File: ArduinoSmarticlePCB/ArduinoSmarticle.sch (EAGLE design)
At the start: 22 parts, among them U1 LSM6DS3DOT_INDICATION

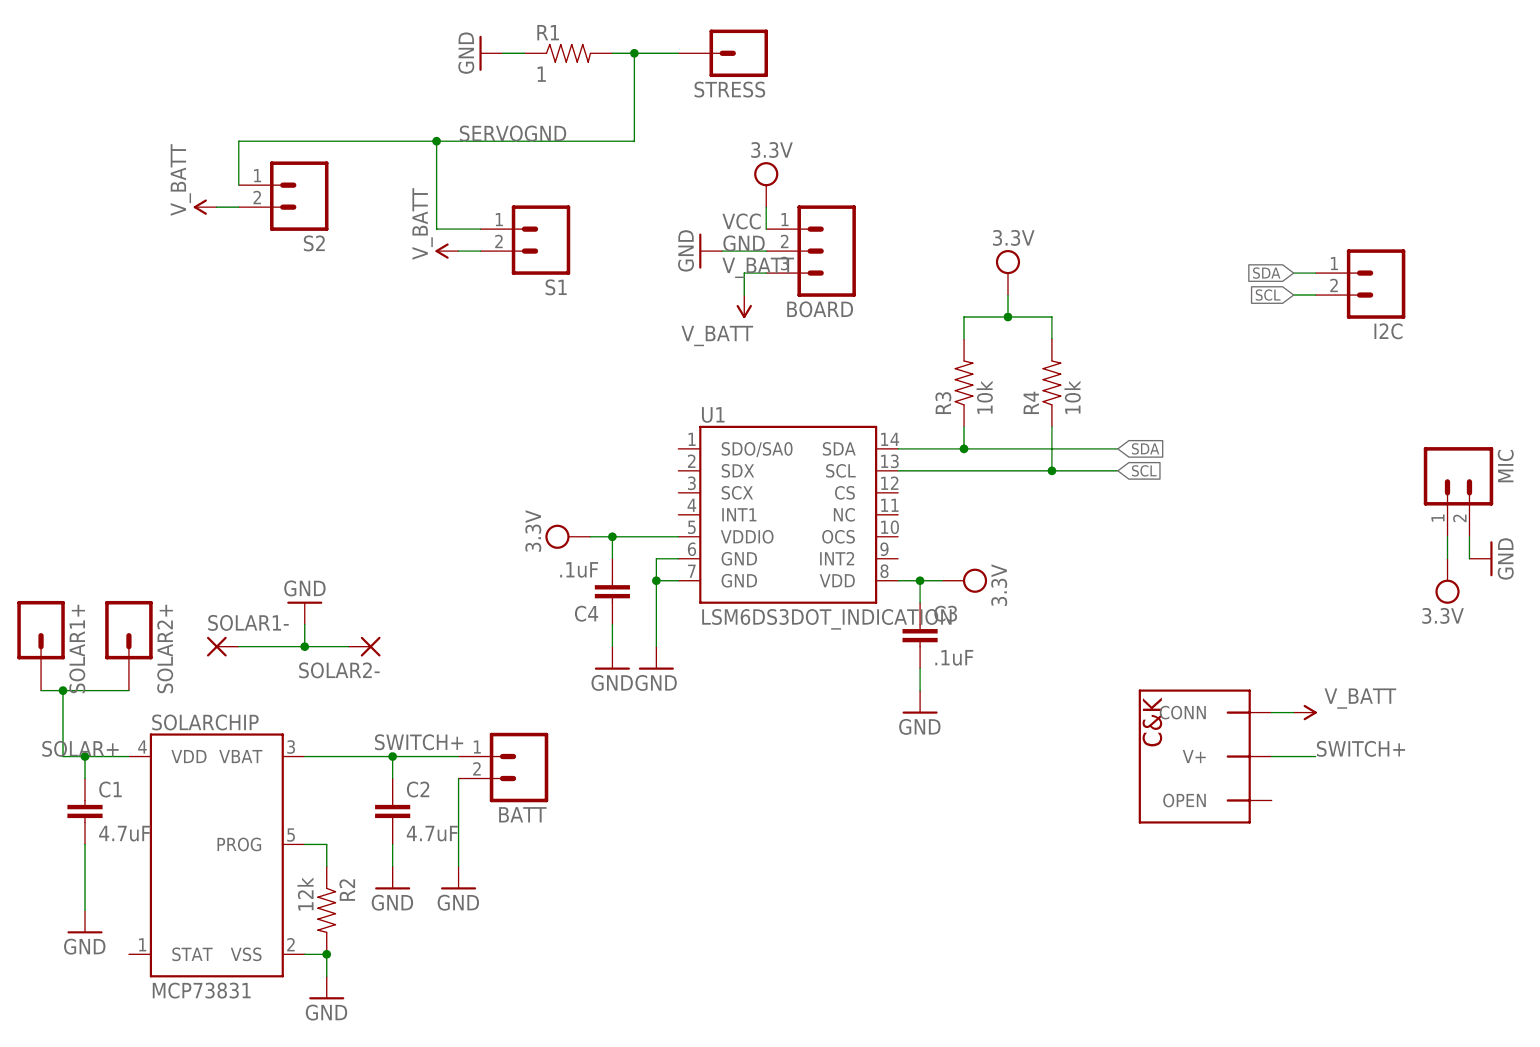
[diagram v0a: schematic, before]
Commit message: improved size of board and isolation size, added mathematica notebook describing solar panels
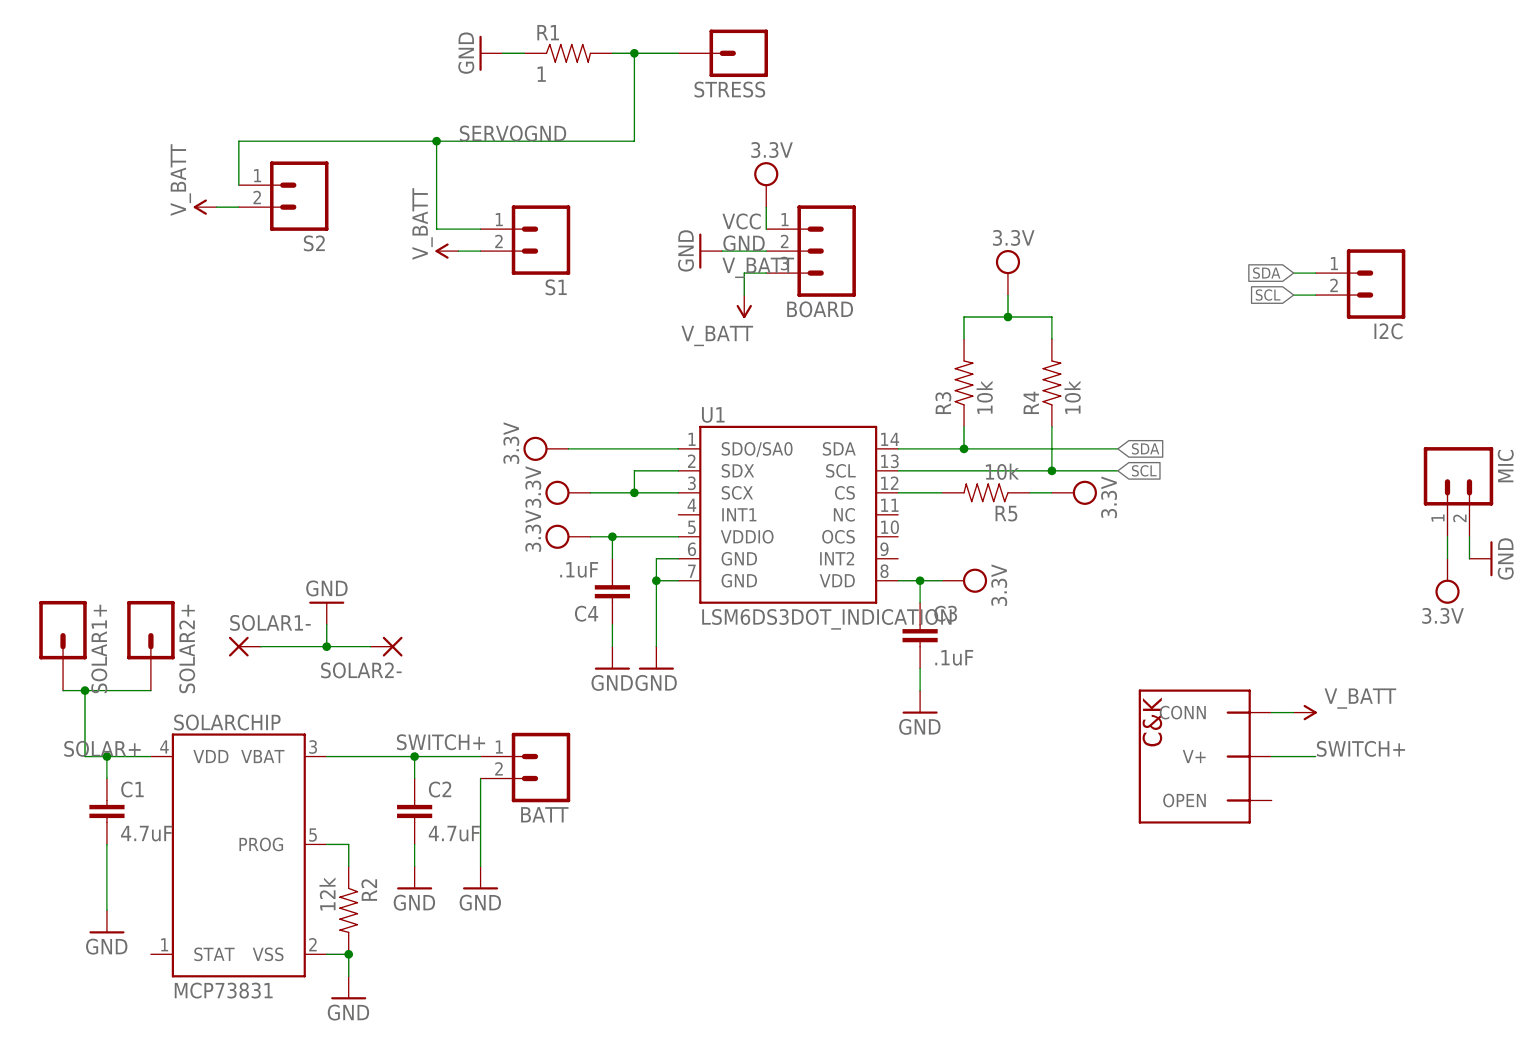
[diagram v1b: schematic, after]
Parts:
- added R5: 10k, SparkFun-Resistors:4.7KOHM-1/10W-1%(0603)
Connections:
- new net N$2: R5.2, U1.CS
- net VCC: now also R5.1, U1.SCX, U1.SDO/SA0, U1.SDX
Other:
- moved on the sheet: BATT, C1, C2, R2, SOLAR1+, SOLAR1-, SOLAR2+, SOLAR2-, SOLARCHIP
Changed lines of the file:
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@@
 <part name="GND11" library="SparkFun-Aesthetics" deviceset="GND" device=""/>
 <part name="I2C" library="SparkFun-Connectors" deviceset="M02" device="PTH"/>
+<part name="R5" library="SparkFun-Resistors" deviceset="4.7KOHM-1/10W-1%(0603)" device="" value="10k"/>
+<part name="3.3V5" library="supply2" deviceset="VCC" device="" value="3.3V"/>
+<part name="3.3V6" library="supply2" deviceset="VCC" device="" value="3.3V"/>
+<part name="3.3V7" library="supply2" deviceset="VCC" device="" value="3.3V"/>
 </parts>
 <sheets>
@@
 <instances>
 <instance part="FRAME1" gate="G$1" x="0" y="0"/>
-<instance part="SOLARCHIP" gate="G$1" x="25.4" y="27.94"/>
-<instance part="C1" gate="G$1" x="10.16" y="30.48"/>
-<instance part="C2" gate="G$1" x="45.72" y="30.48"/>
-<instance part="GND1" gate="1" x="10.16" y="17.78"/>
-<instance part="GND2" gate="1" x="45.72" y="22.86"/>
-<instance part="GND4" gate="1" x="38.1" y="10.16"/>
-<instance part="R2" gate="G$1" x="38.1" y="20.32" rot="R270"/>
+<instance part="SOLARCHIP" gate="G$1" x="27.94" y="27.94"/>
+<instance part="C1" gate="G$1" x="12.7" y="30.48"/>
+<instance part="C2" gate="G$1" x="48.26" y="30.48"/>
+<instance part="GND1" gate="1" x="12.7" y="17.78"/>
+<instance part="GND2" gate="1" x="48.26" y="22.86"/>
+<instance part="GND4" gate="1" x="40.64" y="10.16"/>
+<instance part="R2" gate="G$1" x="40.64" y="20.32" rot="R270"/>
 <instance part="S2" gate="G$1" x="35.56" y="104.14" smashed="yes" rot="R180">
 <attribute name="VALUE" x="38.1" y="111.76" size="1.778" layer="96" rot="R180"/>
@@
 <instance part="GND5" gate="1" x="81.28" y="96.52" rot="R270"/>
 <instance part="SUPPLY4" gate="G$1" x="86.36" y="91.44" rot="R180"/>
-<instance part="BATT" gate="G$1" x="60.96" y="38.1" rot="R180"/>
-<instance part="GND6" gate="1" x="53.34" y="22.86"/>
-<instance part="SOLAR1+" gate="G$1" x="5.08" y="53.34" rot="R270"/>
-<instance part="SOLAR2+" gate="G$1" x="15.24" y="53.34" rot="R270"/>
-<instance part="GND3" gate="1" x="35.56" y="55.88" rot="R180"/>
-<instance part="SOLAR1-" gate="1" x="25.4" y="50.8"/>
-<instance part="SOLAR2-" gate="1" x="43.18" y="50.8" rot="R180"/>
+<instance part="BATT" gate="G$1" x="63.5" y="38.1" rot="R180"/>
+<instance part="GND6" gate="1" x="55.88" y="22.86"/>
+<instance part="SOLAR1+" gate="G$1" x="7.62" y="53.34" rot="R270"/>
+<instance part="SOLAR2+" gate="G$1" x="17.78" y="53.34" rot="R270"/>
+<instance part="GND3" gate="1" x="38.1" y="55.88" rot="R180"/>
+<instance part="SOLAR1-" gate="1" x="27.94" y="50.8"/>
+<instance part="SOLAR2-" gate="1" x="45.72" y="50.8" rot="R180"/>
 <instance part="U$1" gate="G$1" x="132.08" y="30.48"/>
 <instance part="SUPPLY1" gate="G$1" x="149.86" y="43.18" smashed="yes" rot="R270">
@@
 <instance part="GND11" gate="1" x="106.68" y="43.18"/>
 <instance part="I2C" gate="G$1" x="160.02" y="93.98" rot="R180"/>
+<instance part="R5" gate="G$1" x="114.3" y="68.58" rot="R180"/>
+<instance part="3.3V5" gate="G$1" x="124.46" y="68.58" rot="R270"/>
+<instance part="3.3V6" gate="G$1" x="66.04" y="68.58" rot="R90"/>
+<instance part="3.3V7" gate="G$1" x="63.5" y="73.66" rot="R90"/>
 </instances>
 <busses>
@@
 <pinref part="C1" gate="G$1" pin="2"/>
 <pinref part="GND1" gate="1" pin="GND"/>
-<wire x1="10.16" y1="27.94" x2="10.16" y2="20.32" width="0.1524" layer="91"/>
+<wire x1="12.7" y1="27.94" x2="12.7" y2="20.32" width="0.1524" layer="91"/>
 </segment>
 <segment>
 <pinref part="SOLARCHIP" gate="G$1" pin="VSS"/>
 <pinref part="R2" gate="G$1" pin="2"/>
-<wire x1="35.56" y1="15.24" x2="38.1" y2="15.24" width="0.1524" layer="91"/>
+<wire x1="38.1" y1="15.24" x2="40.64" y2="15.24" width="0.1524" layer="91"/>
 <pinref part="GND4" gate="1" pin="GND"/>
-<wire x1="38.1" y1="15.24" x2="38.1" y2="12.7" width="0.1524" layer="91"/>
-<junction x="38.1" y="15.24"/>
+<wire x1="40.64" y1="15.24" x2="40.64" y2="12.7" width="0.1524" layer="91"/>
+<junction x="40.64" y="15.24"/>
 </segment>
 <segment>
 <pinref part="C2" gate="G$1" pin="2"/>
 <pinref part="GND2" gate="1" pin="GND"/>
-<wire x1="45.72" y1="25.4" x2="45.72" y2="27.94" width="0.1524" layer="91"/>
+<wire x1="48.26" y1="25.4" x2="48.26" y2="27.94" width="0.1524" layer="91"/>
 </segment>
 <segment>
@@
 <pinref part="BATT" gate="G$1" pin="2"/>
 <pinref part="GND6" gate="1" pin="GND"/>
-<wire x1="53.34" y1="25.4" x2="53.34" y2="35.56" width="0.1524" layer="91"/>
+<wire x1="55.88" y1="25.4" x2="55.88" y2="35.56" width="0.1524" layer="91"/>
 </segment>
 <segment>
@@
 <segment>
 <pinref part="SOLAR1-" gate="1" pin="P"/>
-<wire x1="35.56" y1="50.8" x2="27.94" y2="50.8" width="0.1524" layer="91"/>
-<junction x="35.56" y="50.8"/>
+<wire x1="38.1" y1="50.8" x2="30.48" y2="50.8" width="0.1524" layer="91"/>
+<junction x="38.1" y="50.8"/>
 <pinref part="SOLAR2-" gate="1" pin="P"/>
-<wire x1="40.64" y1="50.8" x2="35.56" y2="50.8" width="0.1524" layer="91"/>
+<wire x1="43.18" y1="50.8" x2="38.1" y2="50.8" width="0.1524" layer="91"/>
 <pinref part="GND3" gate="1" pin="GND"/>
-<wire x1="35.56" y1="50.8" x2="35.56" y2="53.34" width="0.1524" layer="91"/>
+<wire x1="38.1" y1="50.8" x2="38.1" y2="53.34" width="0.1524" layer="91"/>
 </segment>
 </net>
@@
 <segment>
 <pinref part="SOLARCHIP" gate="G$1" pin="PROG"/>
-<wire x1="35.56" y1="27.94" x2="38.1" y2="27.94" width="0.1524" layer="91"/>
+<wire x1="38.1" y1="27.94" x2="40.64" y2="27.94" width="0.1524" layer="91"/>
 <pinref part="R2" gate="G$1" pin="1"/>
-<wire x1="38.1" y1="27.94" x2="38.1" y2="25.4" width="0.1524" layer="91"/>
+<wire x1="40.64" y1="27.94" x2="40.64" y2="25.4" width="0.1524" layer="91"/>
 </segment>
 </net>
@@
 <junction x="106.68" y="58.42"/>
 <wire x1="106.68" y1="58.42" x2="109.22" y2="58.42" width="0.1524" layer="91"/>
+</segment>
+<segment>
+<pinref part="R5" gate="G$1" pin="1"/>
+<pinref part="3.3V5" gate="G$1" pin="VCC"/>
+<wire x1="121.92" y1="68.58" x2="119.38" y2="68.58" width="0.1524" layer="91"/>
+</segment>
+<segment>
+<pinref part="U1" gate="G$1" pin="SCX"/>
+<wire x1="78.74" y1="68.58" x2="73.66" y2="68.58" width="0.1524" layer="91"/>
+<pinref part="U1" gate="G$1" pin="SDX"/>
+<wire x1="78.74" y1="71.12" x2="73.66" y2="71.12" width="0.1524" layer="91"/>
+<wire x1="73.66" y1="68.58" x2="73.66" y2="71.12" width="0.1524" layer="91"/>
+<junction x="73.66" y="68.58"/>
+<pinref part="3.3V6" gate="G$1" pin="VCC"/>
+<wire x1="68.58" y1="68.58" x2="73.66" y2="68.58" width="0.1524" layer="91"/>
+</segment>
+<segment>
+<pinref part="U1" gate="G$1" pin="SDO/SA0"/>
+<wire x1="78.74" y1="73.66" x2="66.04" y2="73.66" width="0.1524" layer="91"/>
+<pinref part="3.3V7" gate="G$1" pin="VCC"/>
 </segment>
 </net>
@@
 <pinref part="BATT" gate="G$1" pin="1"/>
 <pinref part="SOLARCHIP" gate="G$1" pin="VBAT"/>
-<wire x1="35.56" y1="38.1" x2="45.72" y2="38.1" width="0.1524" layer="91"/>
+<wire x1="38.1" y1="38.1" x2="48.26" y2="38.1" width="0.1524" layer="91"/>
 <pinref part="C2" gate="G$1" pin="1"/>
-<wire x1="45.72" y1="38.1" x2="45.72" y2="35.56" width="0.1524" layer="91"/>
-<junction x="45.72" y="38.1"/>
-<label x="54.102" y="40.64" size="1.778" layer="95" rot="R180"/>
-<wire x1="53.34" y1="38.1" x2="45.72" y2="38.1" width="0.1524" layer="91"/>
+<wire x1="48.26" y1="38.1" x2="48.26" y2="35.56" width="0.1524" layer="91"/>
+<junction x="48.26" y="38.1"/>
+<label x="56.642" y="40.64" size="1.778" layer="95" rot="R180"/>
+<wire x1="55.88" y1="38.1" x2="48.26" y2="38.1" width="0.1524" layer="91"/>
 </segment>
 <segment>
@@
 <segment>
 <pinref part="SOLAR1+" gate="G$1" pin="1"/>
-<wire x1="5.08" y1="45.72" x2="7.62" y2="45.72" width="0.1524" layer="91"/>
-<wire x1="7.62" y1="45.72" x2="7.62" y2="38.1" width="0.1524" layer="91"/>
-<junction x="7.62" y="45.72"/>
+<wire x1="7.62" y1="45.72" x2="10.16" y2="45.72" width="0.1524" layer="91"/>
+<wire x1="10.16" y1="45.72" x2="10.16" y2="38.1" width="0.1524" layer="91"/>
+<junction x="10.16" y="45.72"/>
 <pinref part="SOLARCHIP" gate="G$1" pin="VDD"/>
 <pinref part="C1" gate="G$1" pin="1"/>
-<wire x1="10.16" y1="38.1" x2="15.24" y2="38.1" width="0.1524" layer="91"/>
-<wire x1="10.16" y1="38.1" x2="10.16" y2="35.56" width="0.1524" layer="91"/>
-<junction x="10.16" y="38.1"/>
-<label x="5.08" y="38.1" size="1.778" layer="95"/>
-<wire x1="7.62" y1="38.1" x2="10.16" y2="38.1" width="0.1524" layer="91"/>
+<wire x1="12.7" y1="38.1" x2="17.78" y2="38.1" width="0.1524" layer="91"/>
+<wire x1="12.7" y1="38.1" x2="12.7" y2="35.56" width="0.1524" layer="91"/>
+<junction x="12.7" y="38.1"/>
+<label x="7.62" y="38.1" size="1.778" layer="95"/>
+<wire x1="10.16" y1="38.1" x2="12.7" y2="38.1" width="0.1524" layer="91"/>
 <pinref part="SOLAR2+" gate="G$1" pin="1"/>
-<wire x1="15.24" y1="45.72" x2="7.62" y2="45.72" width="0.1524" layer="91"/>
-</segment>
-</net>
+<wire x1="17.78" y1="45.72" x2="10.16" y2="45.72" width="0.1524" layer="91"/>
+</segment>
+</net>
+<net name="N$2" class="0">
+<segment>
+<pinref part="U1" gate="G$1" pin="CS"/>
+<pinref part="R5" gate="G$1" pin="2"/>
+<wire x1="104.14" y1="68.58" x2="109.22" y2="68.58" width="0.1524" layer="91"/>
+</segment>
+</net>
